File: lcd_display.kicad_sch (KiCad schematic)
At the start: 1 part, among them P1 OrangePi-2G-IOT LCD Interface

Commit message: Continue schematic work
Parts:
- added C1, C2, C3, C4: 100n/50V, Capacitors_Smd_0603:100nF_0603, symbol Capacitors_Smd0603:100n
- added C5: 1uF/6V3, Capacitors_Smd_0603:1uF_0603, symbol Capacitors_Smd0603:1uF_0603
- added C6, C7: 100nF/50V, Capacitors_Smd_0603:100nF_0603, symbol Capacitors_Smd0603:100n
- added C8: 4.7uF/35V, Capacitors_Smd_0603:4_7uF_0603, symbol Capacitors_Smd0603:4_7uF_0603
- added D1: NSR0530H-D, Diodes:NSR0530H-D_SOD323, symbol Diodes:NSR0530H-D
- added L1: 4u7H_CD32_SMD_Coil, Inductors:4u7H_SMD_CD32, symbol Inductors:4u7H_CD32_SMD_Coil
- added R1: 10k, Resistor_Smd_0603:10k_0603, symbol Resistors_Smd0603:10k
- added R2, R3, R4, R5: 1k, Resistor_Smd_0603:1k_0603, symbol Resistors_Smd0603:1k_0603
- added R6: 10R/1%/0.1Wat, Resistor_Smd_0603:10R_0603, symbol Resistors_Smd0603:10R_1%
- added U1, U2, U3, U4: 82357120100, ESD_Protectors:82357120100, symbol esd_protectors:82357120100
- added U7: TPS61169DCKR, Lcd_Backlight_Drivers:TPS61169DCKR, symbol Lcd_Backlight_Drivers:TPS61169DCKR
- added U8: AP2127K-2.8TRG1, Linear:AP2127K-2.8TRG1_SOT23, symbol Linear_Regulators:AP2127K-2.8TRG1
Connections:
- net LCD_D1(B2): now reaches P1.10 (P10)
- net LCD_D2(B3): now reaches P1.11 (P1)
- net LCD_D3(B4): now reaches P1.12 (P2)
- net LCD_D4(B5): now reaches P1.13 (P3)
- net LCD_D5(G0): now reaches P1.14 (P4)
- net LCD_D6(G1): now reaches P1.15 (P5)
- net LCD_D7(G2): now reaches P1.16 (P6)
- net LCD_D8(G3): now reaches P1.17 (P7)
- net LCD_D9(G4): now reaches P1.18 (P8)
- net LCD_D10(G5): now reaches P1.19 (P9)
- net at P1.2 (P2): now also C3.1
- net LCD_D11(R1): now reaches P1.20 (P10)
- net LCD_D12(R2): now reaches P1.21 (P1)
- net LCD_D13(R3): now reaches P1.22 (P2)
- net LCD_D14(R4): now reaches P1.23 (P3)
- net LCD_D15(R5): now reaches P1.24 (P4)
- net LCD_CS: now reaches P1.25 (P5)
- net LCD_WR(DE): now reaches P1.26 (P6)
- net LCD_FMARK(PCLK): now reaches P1.27 (P7)
- net LCD_RS(HSYNC): now reaches P1.28 (P8)
- net LCD_RD(VSYNC): now reaches P1.29 (P9)
- net GND: now reaches P1.3 (P3)
- net GND: now also P1.31 (P1), P1.33 (P3), P1.35 (P5), P1.8 (P8), C1.2, C2.2, C3.2, C4.2, C5.2, C6.2, C7.2, C8.2, R6.2, U1.1 (A), U2.1 (A), U3.1 (A), U4.1 (A), U7.2 (GND), U8.1 (Adj(GND))
- net LCD_RST: now reaches P1.30 (P10)
- net 2V8: now reaches P1.32 (P2)
- net 2V8: now also P1.36 (P6), P1.4 (P4), C1.1, C2.1, C4.1, C7.1, R1.1, U8.2 (Vout)
- net at P1.37 (P7): now also R3.2, U1.2 (K)
- net at P1.38 (P8): now also R4.2, U2.2 (K)
- net at P1.39 (P9): now also R2.2, U3.2 (K)
- net at P1.40 (P10): now also R5.2, U4.2 (K)
- net LCD_SPI_CS0: now reaches P1.5 (P5)
- net LCD_SPI_CLK: now reaches P1.6 (P6)
- net LCD_SPI_DIO: now reaches P1.7 (P7)
- net LCD_D0(B1): now reaches P1.9 (P9)
- new net: D1.2 (A), L1.2, U7.1 (SW)
- new net BACKLIGHT_HIGH: C8.1, D1.1 (K)
- new net BACKLIGHT_LOW: R6.1, U7.3 (FB)
- new net BACKLIGHT_PWM: U7.4 (CTRL)
- new net POWER_SUPPLY_2.7-5.5V: C5.1, C6.1, L1.1, U7.5 (VIN), U8.3 (Vin)
- new net TP_I2C_SCL: R4.1
- new net TP_I2C_SDA: R3.1
- new net TP_IRQ: R1.2, R2.1
- new net TP_SHUTDOWN: R5.1
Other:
- note added: "CS"
- note added: "D0(B1)"
- note added: "D1(B2)"
- note added: "D10(G5)"
- note added: "D11(R1)"
- note added: "D12(R2)"
- note added: "D13(R3)"
- note added: "D14(R4)"
- note added: "D15(R5)"
- note added: "D2(B3)"
- note added: "D3(B4)"
- note added: "D4(B5)"
- note added: "D5(G0)"
- note added: "D6(G1)"
- note added: "D7(G2)"
- note added: "D8(G3)"
- note added: "D9(G4)"
- note added: "FMARK(PCLK)"
- note added: "GND"
- note added: "IOVDD"
- note added: "LED+(P)"
- note added: "LED-(P)"
- note added: "RD(VSYNC)"
- note added: "RS(HSYNC)"
- note added: "RST"
- note added: "SPI_CLK"
- note added: "SPI_CS"
- note added: "SPI_DO"
- note added: "TP_INT"
- note added: "TP_RST"
- note added: "TP_SCL"
- note added: "TP_SDA"
- note added: "TP_VDD"
- note added: "VDD"
- note added: "VLED+(S)"
- note added: "VLED-(S)"
- note added: "WR(DE)"
- moved on the sheet: P1

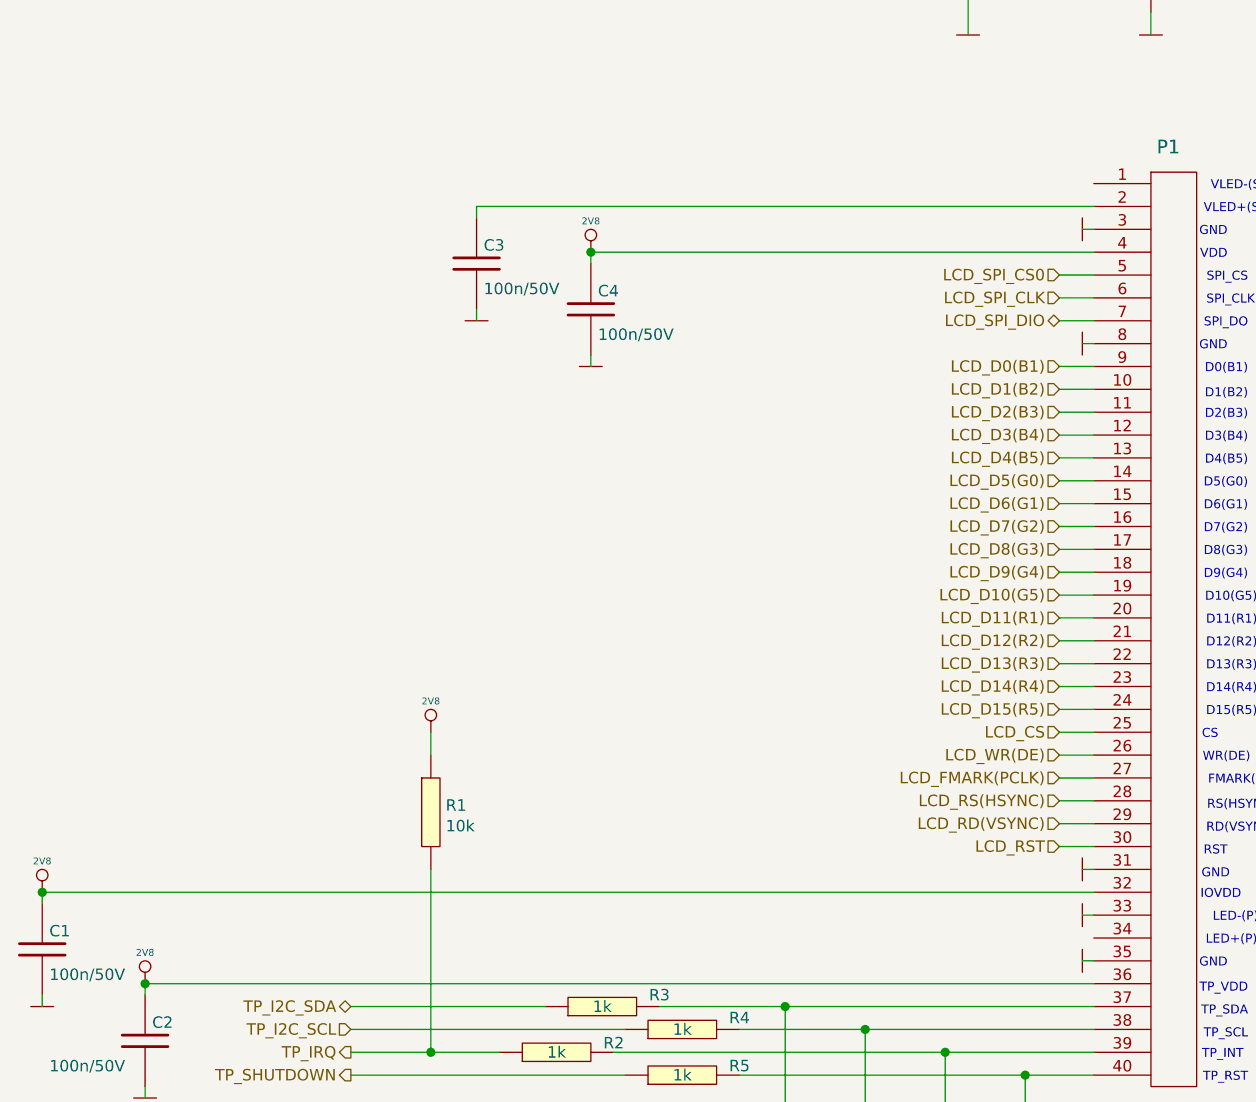
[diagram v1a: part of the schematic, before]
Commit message: Corrected schematic and added new elements
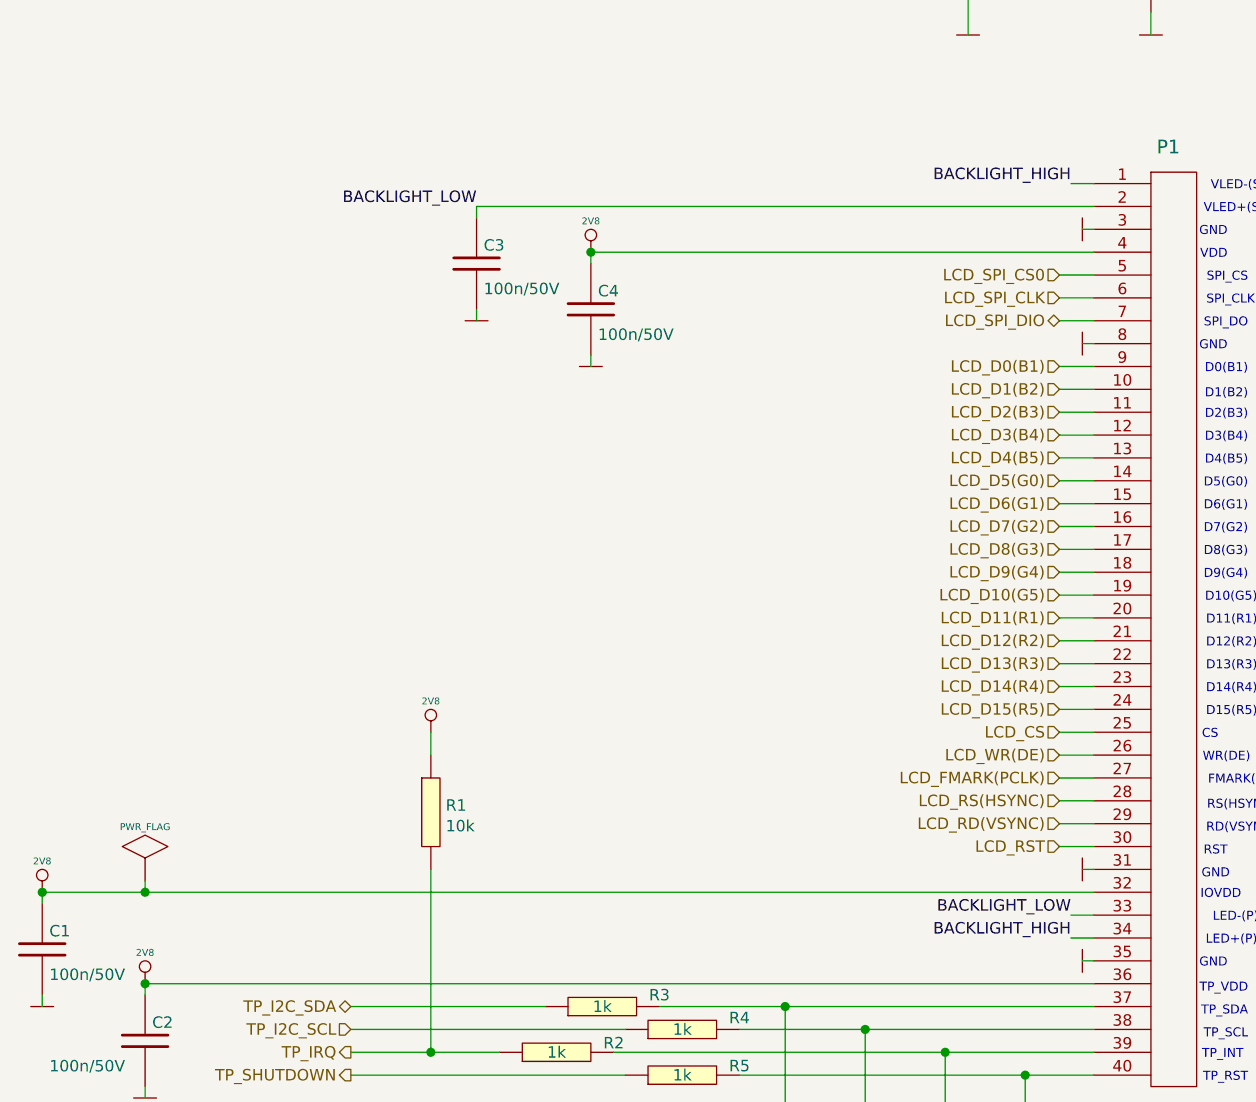
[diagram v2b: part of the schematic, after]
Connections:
- net BACKLIGHT_HIGH: now also P1.1 (P1), P1.34 (P4)
- net BACKLIGHT_LOW: now also C3.1, P1.2 (P2), P1.33 (P3)
- net GND: no longer P1.33 (P3)
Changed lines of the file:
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@@
   )
   (junction (at 101.6 217.17) (diameter 1.016) (color 0 0 0 0))
+  (junction (at 113.03 217.17) (diameter 1.016) (color 0 0 0 0))
   (junction (at 113.03 227.33) (diameter 1.016) (color 0 0 0 0))
   (junction (at 144.78 234.95) (diameter 1.016) (color 0 0 0 0))
@@
     (stroke (width 0) (type solid) (color 0 0 0 0))
   )
-  (wire (pts (xy 101.6 217.17) (xy 218.44 217.17))
+  (wire (pts (xy 101.6 217.17) (xy 113.03 217.17))
     (stroke (width 0) (type solid) (color 0 0 0 0))
   )
@@
     (stroke (width 0) (type solid) (color 0 0 0 0))
   )
+  (wire (pts (xy 113.03 215.9) (xy 113.03 217.17))
+    (stroke (width 0) (type solid) (color 0 0 0 0))
+  )
+  (wire (pts (xy 113.03 217.17) (xy 218.44 217.17))
+    (stroke (width 0) (type solid) (color 0 0 0 0))
+  )
   (wire (pts (xy 113.03 227.33) (xy 113.03 228.6))
     (stroke (width 0) (type solid) (color 0 0 0 0))
@@
     (stroke (width 0) (type solid) (color 0 0 0 0))
   )
+  (wire (pts (xy 215.9 138.43) (xy 218.44 138.43))
+    (stroke (width 0) (type solid) (color 0 0 0 0))
+  )
+  (wire (pts (xy 215.9 222.25) (xy 218.44 222.25))
+    (stroke (width 0) (type solid) (color 0 0 0 0))
+  )
   (wire (pts (xy 217.17 48.26) (xy 210.82 48.26))
     (stroke (width 0) (type solid) (color 0 0 0 0))
@@
     (stroke (width 0) (type solid) (color 0 0 0 0))
   )
-  (wire (pts (xy 218.44 219.71) (xy 217.17 219.71))
+  (wire (pts (xy 218.44 219.71) (xy 215.9 219.71))
     (stroke (width 0) (type solid) (color 0 0 0 0))
   )
@@
   (text "FMARK(PCLK)" (at 240.411 205.359 180)
     (effects (font (size 1 1)) (justify right bottom))
+  )
+  (label "BACKLIGHT_LOW" (at 149.86 140.97 180)
+    (effects (font (size 1.27 1.27)) (justify right bottom))
+  )
+  (label "BACKLIGHT_HIGH" (at 215.9 138.43 180)
+    (effects (font (size 1.27 1.27)) (justify right bottom))
+  )
+  (label "BACKLIGHT_LOW" (at 215.9 219.71 180)
+    (effects (font (size 1.27 1.27)) (justify right bottom))
+  )
+  (label "BACKLIGHT_HIGH" (at 215.9 222.25 180)
+    (effects (font (size 1.27 1.27)) (justify right bottom))
   )
   (label "BACKLIGHT_HIGH" (at 294.64 48.26 0)
@@
     )
     (property "Datasheet" "" (id 3) (at 217.17 214.63 0)
-      (effects (font (size 1.524 1.524)))
-    )
-    (pin "1")
-  )
-  (symbol (lib_id "power:GND") (at 217.17 219.71 270) (unit 1)
-    (in_bom yes) (on_board yes) (fields_autoplaced)
-    (property "Reference" "#PWR0141" (id 0) (at 218.44 220.98 0)
-      (effects (font (size 0.762 0.762)) hide)
-    )
-    (property "Value" "GND" (id 1) (at 214.63 219.71 0)
-      (effects (font (size 0.762 0.762)) hide)
-    )
-    (property "Footprint" "" (id 2) (at 217.17 219.71 0)
-      (effects (font (size 1.524 1.524)))
-    )
-    (property "Datasheet" "" (id 3) (at 217.17 219.71 0)
       (effects (font (size 1.524 1.524)))
     )
@@
     (pin "2")
   )
+  (symbol (lib_id "power:PWR_FLAG") (at 113.03 215.9 0) (unit 1)
+    (in_bom yes) (on_board yes) (fields_autoplaced)
+    (property "Reference" "#FLG0101" (id 0) (at 114.3 214.63 0)
+      (effects (font (size 0.762 0.762)) hide)
+    )
+    (property "Value" "PWR_FLAG" (id 1) (at 113.03 209.9107 0)
+      (effects (font (size 0.762 0.762)))
+    )
+    (property "Footprint" "" (id 2) (at 113.03 215.9 0)
+      (effects (font (size 1.524 1.524)))
+    )
+    (property "Datasheet" "" (id 3) (at 113.03 215.9 0)
+      (effects (font (size 1.524 1.524)))
+    )
+    (pin "1")
+  )
   (symbol (lib_id "Diodes:NSR0530H-D") (at 246.38 48.26 0) (unit 1)

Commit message: Finalized project
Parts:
- added R20, R21, R22: 0R, Resistor_Smd_0603:0R_0603, symbol Resistors_Smd0603:0R
- C8: symbol Capacitors_Smd0603:4_7uF_0603 -> Capacitors_Smd0603:4.7uF; LCSC Part # (optional) (none) -> C307467
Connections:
- net BACKLIGHT_HIGH: now also R20.1; no longer P1.1 (P1), P1.34 (P4)
- net POWER_SUPPLY_2.7-5.5V: now also R21.2
- new net: P1.34 (P4), R22.2
- new net BACKLIGHT_VDD: P1.1 (P1), R20.2, R21.1, R22.1
